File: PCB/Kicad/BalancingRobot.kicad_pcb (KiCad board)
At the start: 2 copper layers, 10 parts, among them P1 PWM, P2 BT_USB, P3 CONN_1, P4 CONN_1, P5 CONN_1, P6 CONN_1, U1 74HC00, U2 GY-521, U3 XL7105-SY

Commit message: primera version del PCB
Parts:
- added C1: 0.1u, c_1206, B.Cu at (127.9, 85.1)
- added C2: 10u, C1V5, F.Cu at (152.5, 108.8)
- added C3: 0.1u, c_tant_B, B.Cu at (147.4, 119.8)
- added C4: 10u, c_tant_B, B.Cu at (120.7, 81.0)
- added D1: DIODE, D3, F.Cu at (141.9, 97.3)
- added JP1: JUMPER, SM0603, B.Cu at (116.6, 85.0)
- added P7: CONN_2, PIN_ARRAY_2X1, F.Cu at (152.7, 120.7)
- added P8: PWR, PIN_ARRAY_2X1, F.Cu at (111.6, 80.1)
- added R1: R, R2, F.Cu at (151.3, 102.9)
- added R2: R, R2, F.Cu at (154.6, 102.9)
- added R3: R, R2, F.Cu at (152.5, 115.3)
- added U?1: MCP1700T-33, sot89, B.Cu at (115.7, 81.5)
- P1: footprint PIN_ARRAY_5x1 -> PIN_ARRAY-6X1
- moved P4 3.05 mm to (152.9, 67.6)
- moved P6 3.05 mm to (152.9, 125.0)
- moved P1 2.84 mm to (138.7, 123.4)
- moved U2 1.52 mm to (132.8, 72.8)
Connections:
- APM1 pad 19: (no net) -> BAT
- APM1 pad 5: (no net) -> SCS
- APM1 pad 6: SCS -> SCK
- APM1 pad 7: SCK -> SDIO
- APM1 pad 8: SDIO -> GIO
- APM1 pad 9: GIO -> EN_HB
- P1 pad 1: /PWM2A -> EN_HB
- P1 pad 2: /PWM2B -> /PWM2A
- P1 pad 3: /PWM1A -> /PWM2B
- P1 pad 4: /PWM1B -> /PWM1A
- P1 pad 5: GND -> /PWM1B
- P2 pad 1: RST -> /DTR
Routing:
- net (no net): track 0.00 -> 230.6 mm
- net EN_HB: track 0.00 -> 17.9 mm
- net N-0000015: track 0.00 -> 11.2 mm
- net N-0000013: track 0.00 -> 9.72 mm
- net BAT: track 0.00 -> 9.71 mm
- net RST: track 21.2 -> 13.5 mm
- net /DTR: track 0.00 -> 4.83 mm
- net VCC: track 104.9 -> 108.7 mm
- net N-000005: track 0.00 -> 3.27 mm
- net SCS: track 24.9 -> 27.5 mm
- net /PWM2B: track 14.7 -> 17.3 mm
- net /PWM2A: track 10.5 -> 13.1 mm
- net /PWM1B: track 10.9 -> 13.5 mm
- net /PWM1A: track 15.7 -> 18.2 mm
- net /SCL: track 30.3 -> 28.3 mm
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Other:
- board text added: "ANTENA"

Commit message: Diagramas
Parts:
- moved C4 0.76 mm to (120.7, 80.3)
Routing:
- net VCC: track 108.7 -> 110.1 mm
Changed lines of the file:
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@@
     (thickness 1.6)
     (drawings 7)
-    (tracks 164)
+    (tracks 166)
     (zones 0)
     (modules 22)
@@
   )
   (setup
-    (last_trace_width 0.254)
+    (last_trace_width 1.016)
     (user_trace_width 0.381)
     (user_trace_width 0.508)
@@
   )
   (module c_tant_B (layer B.Cu)
-    (at 120.65 81.026 270)
+    (at 120.65 80.264 270)
     (descr "SMT capacitor, tantalum size B")
     (fp_text reference C4 (at 0 1.9685 270) (layer B.SilkS)
@@
   (segment (start 116.459 113.03) (end 124.46 105.029) (width 0.762) (layer B.Cu) (net 26))
   (segment (start 121.666 87.63) (end 132.08 87.63) (width 1.524) (layer B.Cu) (net 27))
+  (segment (start 120.65 81.788) (end 120.65 82.169) (width 1.016) (layer B.Cu) (net 28) (status C00000))
+  (segment (start 120.65 82.169) (end 119.888 82.931) (width 1.016) (layer B.Cu) (net 28) (status 400000))
   (segment (start 119.888 82.931) (end 117.70106 82.931) (width 1.143) (layer B.Cu) (net 28))
   (segment (start 117.70106 82.931) (end 117.59692 83.03514) (width 1.143) (layer B.Cu) (net 28))
@@
     )
   )
-  (zone (net 0) (net_name "") (layer B.Cu) (hatch edge 0.508)
+  (zone (net 0) (net_name "") (layer B.Cu) (hatch full 0.508)
     (connect_pads (clearance 0.508))
     (min_thickness 0.254)

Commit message: v1 del PCB y diagrama, primera version construida
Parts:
- P1: footprint PIN_ARRAY-6X1 -> PINHEAD1-8
- moved P7 4.46 mm to (154.2, 116.5), turned to 90 degrees
- moved R3 1.28 mm to (151.3, 115.2)
- moved P1 1.14 mm to (138.7, 124.6)
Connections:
- P1 pad 1: EN_HB -> GND
- P1 pad 2: /PWM2A -> EN_HB
- P1 pad 3: /PWM2B -> /PWM2A
- P1 pad 4: /PWM1A -> /PWM2B
- P1 pad 5: /PWM1B -> /PWM1A
- P1 pad 6: GND -> /PWM1B
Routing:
- net VCC: track 110.1 -> 118.9 mm
- net GND: track 0.00 -> 3.35 mm
- net /PWM1B: track 13.5 -> 14.6 mm
- net EN_HB: track 17.9 -> 19.1 mm
- net /PWM2B: track 17.3 -> 18.4 mm
- net /PWM2A: track 13.1 -> 14.2 mm
- net /PWM1A: track 18.2 -> 19.4 mm
- net N-000007: track 11.2 -> 10.5 mm

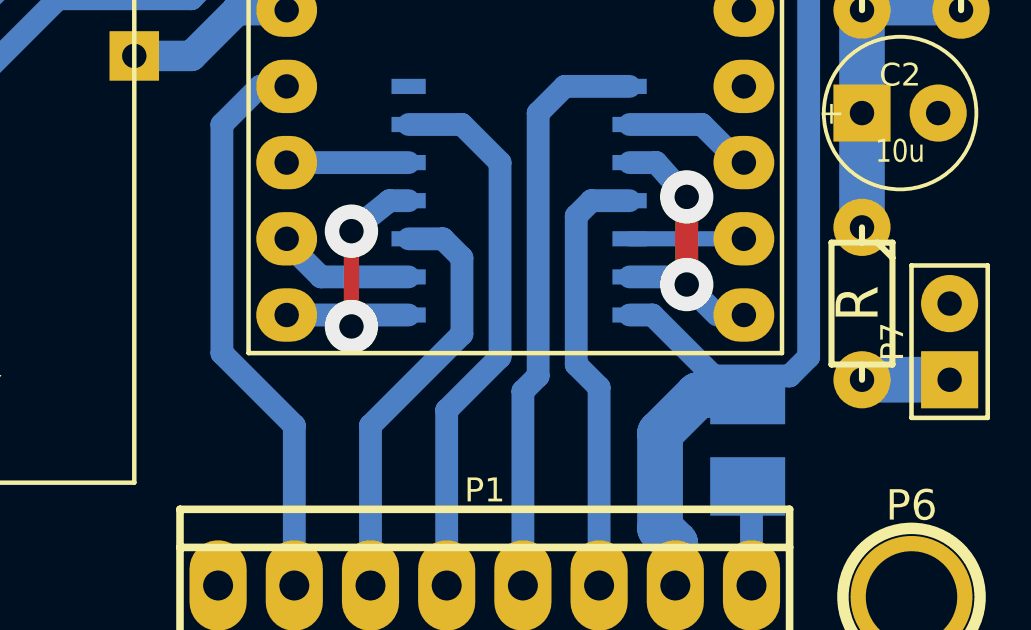
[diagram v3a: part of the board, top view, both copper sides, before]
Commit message: Se agregaron resistencias pulldown en las señales PWM para que no se active el driver mientras el micro se esta iniciando
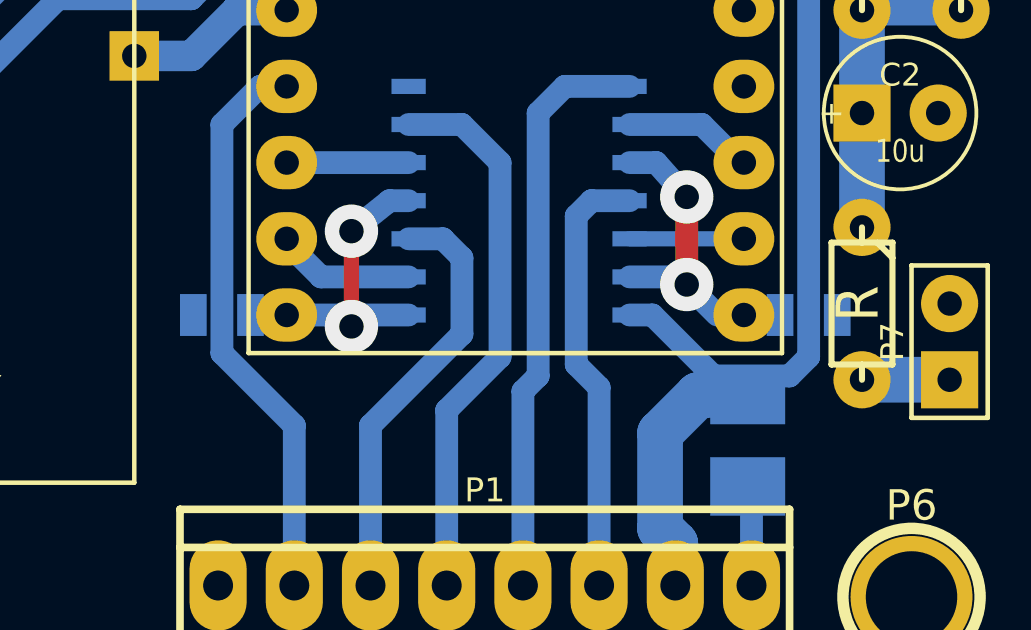
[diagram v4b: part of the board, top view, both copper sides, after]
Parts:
- added R4: 10k, SM0805, B.Cu at (149.5, 115.6)
- added R5: 10k, SM0805, B.Cu at (129.9, 115.6)
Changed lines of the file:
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@@
 (kicad_pcb (version 3) (host pcbnew "(22-Jun-2014 BZR 4027)-stable")
   (general
-    (links 63)
-    (no_connects 0)
-    (area 98.87043 55.062001 166.686571 133.256)
+    (links 67)
+    (no_connects 4)
+    (area 0 0 0 0)
     (thickness 1.6)
     (drawings 7)
     (tracks 171)
     (zones 0)
-    (modules 22)
+    (modules 24)
     (nets 29)
   )
@@
   )
   (setup
-    (last_trace_width 1.524)
+    (last_trace_width 0.762)
     (user_trace_width 0.381)
     (user_trace_width 0.508)
@@
   (net 15 GND)
   (net 16 INT)
-  (net 17 N-0000013)
-  (net 18 N-000006)
-  (net 19 N-000007)
+  (net 17 N-0000011)
+  (net 18 N-000002)
+  (net 19 N-000009)
   (net 20 PWM1)
   (net 21 PWM2)
@@
     (add_net GND)
     (add_net INT)
-    (add_net N-0000013)
-    (add_net N-000006)
-    (add_net N-000007)
+    (add_net N-0000011)
+    (add_net N-000002)
+    (add_net N-000009)
     (add_net PWM1)
     (add_net PWM2)
@@
     (pad 1 thru_hole rect (at -1.27 0 90) (size 1.905 1.905) (drill 0.8128)
       (layers *.Cu *.Mask F.SilkS)
-      (net 18 N-000006)
+      (net 18 N-000002)
     )
     (pad 2 thru_hole circle (at 1.27 0 90) (size 1.905 1.905) (drill 0.8128)
@@
     (pad 1 thru_hole rect (at -1.27 0) (size 1.905 1.905) (drill 0.8128)
       (layers *.Cu *.Mask F.SilkS)
-      (net 19 N-000007)
+      (net 19 N-000009)
     )
     (pad 2 thru_hole circle (at 1.27 0) (size 1.905 1.905) (drill 0.8128)
@@
     (pad 1 thru_hole circle (at -2.54 0 270) (size 1.905 1.905) (drill 0.8128)
       (layers *.Cu *.Mask F.SilkS)
-      (net 19 N-000007)
+      (net 19 N-000009)
     )
     (pad 2 thru_hole circle (at 2.54 0 270) (size 1.905 1.905) (drill 0.8128)
       (layers *.Cu *.Mask F.SilkS)
-      (net 18 N-000006)
+      (net 18 N-000002)
     )
     (model discret/resistor.wrl
@@
     (pad 2 thru_hole circle (at 2.54 0 270) (size 1.905 1.905) (drill 0.8128)
       (layers *.Cu *.Mask F.SilkS)
-      (net 19 N-000007)
+      (net 19 N-000009)
     )
     (model discret/resistor.wrl
@@
     (pad 2 thru_hole circle (at 2.54 0 270) (size 1.905 1.905) (drill 0.8128)
       (layers *.Cu *.Mask F.SilkS)
-      (net 19 N-000007)
+      (net 19 N-000009)
     )
     (model discret/resistor.wrl
@@
     (pad 1 thru_hole rect (at -1.27 0 90) (size 1.905 1.905) (drill 0.8128)
       (layers *.Cu *.Mask F.SilkS)
-      (net 17 N-0000013)
+      (net 17 N-0000011)
     )
     (pad 2 thru_hole circle (at 1.27 0 90) (size 1.905 1.905) (drill 0.8128)
@@
     (pad 2 smd rect (at 0 -1.651 270) (size 0.70104 2.10058)
       (layers B.Cu B.Paste B.Mask)
-      (net 17 N-0000013)
+      (net 17 N-0000011)
     )
     (pad 3 smd rect (at 1.50114 -1.89992 270) (size 0.70104 1.6002)
@@
     (pad 2 smd rect (at 0 0.7493 270) (size 1.99898 2.75082)
       (layers B.Cu B.Paste B.Mask)
-      (net 17 N-0000013)
+      (net 17 N-0000011)
     )
     (model smd/smd_transistors/sot89.wrl
@@
     (pad 1 smd rect (at -0.381 0) (size 0.635 1.143)
       (layers B.Cu B.Paste B.Mask)
-      (net 17 N-0000013)
+      (net 17 N-0000011)
     )
     (pad 2 smd rect (at 0.762 0) (size 0.635 1.143)
@@
       (layers *.Cu *.Mask F.SilkS)
       (net 15 GND)
+    )
+  )
+  (module SM0805 (layer B.Cu)
+    (at 149.479 115.57 180)
+    (attr smd)
+    (fp_text reference R4 (at 0 0.3175 180) (layer B.SilkS)
+      (effects (font (size 0.50038 0.50038) (thickness 0.10922)) (justify mirror))
+    )
+    (fp_text value 10k (at 0 -0.381 180) (layer B.SilkS)
+      (effects (font (size 0.50038 0.50038) (thickness 0.10922)) (justify mirror))
+    )
+    (fp_circle (center -1.651 -0.762) (end -1.651 -0.635) (layer B.SilkS) (width 0.09906))
+    (fp_line (start -0.508 -0.762) (end -1.524 -0.762) (layer B.SilkS) (width 0.09906))
+    (fp_line (start -1.524 -0.762) (end -1.524 0.762) (layer B.SilkS) (width 0.09906))
+    (fp_line (start -1.524 0.762) (end -0.508 0.762) (layer B.SilkS) (width 0.09906))
+    (fp_line (start 0.508 0.762) (end 1.524 0.762) (layer B.SilkS) (width 0.09906))
+    (fp_line (start 1.524 0.762) (end 1.524 -0.762) (layer B.SilkS) (width 0.09906))
+    (fp_line (start 1.524 -0.762) (end 0.508 -0.762) (layer B.SilkS) (width 0.09906))
+    (pad 1 smd rect (at -0.9525 0 180) (size 0.889 1.397)
+      (layers B.Cu B.Paste B.Mask)
+      (net 15 GND)
+    )
+    (pad 2 smd rect (at 0.9525 0 180) (size 0.889 1.397)
+      (layers B.Cu B.Paste B.Mask)
+      (net 21 PWM2)
+    )
+    (model smd/chip_cms.wrl
+      (at (xyz 0 0 0))
+      (scale (xyz 0.1 0.1 0.1))
+      (rotate (xyz 0 0 0))
+    )
+  )
+  (module SM0805 (layer B.Cu)
+    (at 129.921 115.57)
+    (attr smd)
+    (fp_text reference R5 (at 0 0.3175) (layer B.SilkS)
+      (effects (font (size 0.50038 0.50038) (thickness 0.10922)) (justify mirror))
+    )
+    (fp_text value 10k (at 0 -0.381) (layer B.SilkS)
+      (effects (font (size 0.50038 0.50038) (thickness 0.10922)) (justify mirror))
+    )
+    (fp_circle (center -1.651 -0.762) (end -1.651 -0.635) (layer B.SilkS) (width 0.09906))
+    (fp_line (start -0.508 -0.762) (end -1.524 -0.762) (layer B.SilkS) (width 0.09906))
+    (fp_line (start -1.524 -0.762) (end -1.524 0.762) (layer B.SilkS) (width 0.09906))
+    (fp_line (start -1.524 0.762) (end -0.508 0.762) (layer B.SilkS) (width 0.09906))
+    (fp_line (start 0.508 0.762) (end 1.524 0.762) (layer B.SilkS) (width 0.09906))
+    (fp_line (start 1.524 0.762) (end 1.524 -0.762) (layer B.SilkS) (width 0.09906))
+    (fp_line (start 1.524 -0.762) (end 0.508 -0.762) (layer B.SilkS) (width 0.09906))
+    (pad 1 smd rect (at -0.9525 0) (size 0.889 1.397)
+      (layers B.Cu B.Paste B.Mask)
+      (net 15 GND)
+    )
+    (pad 2 smd rect (at 0.9525 0) (size 0.889 1.397)
+      (layers B.Cu B.Paste B.Mask)
+      (net 20 PWM1)
+    )
+    (model smd/chip_cms.wrl
+      (at (xyz 0 0 0))
+      (scale (xyz 0.1 0.1 0.1))
+      (rotate (xyz 0 0 0))
     )
   )
@@
   (segment (start 111.633 81.407) (end 114.8207 81.407) (width 1.524) (layer B.Cu) (net 17))
   (segment (start 114.8207 81.407) (end 114.9477 81.534) (width 1.524) (layer B.Cu) (net 17))
-  (segment (start 154.178 117.729) (end 151.257 117.729) (width 1.524) (layer B.Cu) (net 18) (status C00000))
-  (segment (start 151.257 112.649) (end 151.257 108.839) (width 1.524) (layer B.Cu) (net 19) (status C00000))
+  (segment (start 154.178 117.729) (end 151.257 117.729) (width 1.524) (layer B.Cu) (net 18))
+  (segment (start 151.257 112.649) (end 151.257 108.839) (width 1.524) (layer B.Cu) (net 19))
   (segment (start 151.257 108.839) (end 151.257 105.41) (width 1.524) (layer B.Cu) (net 19))
   (segment (start 151.257 105.41) (end 154.559 105.41) (width 1.016) (layer B.Cu) (net 19))
